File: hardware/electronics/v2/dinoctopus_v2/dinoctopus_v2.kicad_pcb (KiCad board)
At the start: 2 copper layers, 67 parts, among them J1 Conn_01x04_Socket, J1-I1 SJ-3524-SMT, J1-I2 SJ-3524-SMT, J1-I3 SJ-3524-SMT, J1-I4 SJ-3524-SMT, J1-I5 SJ-3524-SMT, J11-O1 SJ-3524-SMT, J11-O2 SJ-3524-SMT, J11-O3 SJ-3524-SMT, J11-O4 SJ-3524-SMT, J11-O5 SJ-3524-SMT, J2 Conn_01x03_Pin, U1 Pico mounting, U2 H11L1, U3 H11L1, U4 H11L1, U5 H11L1, U6 H11L1

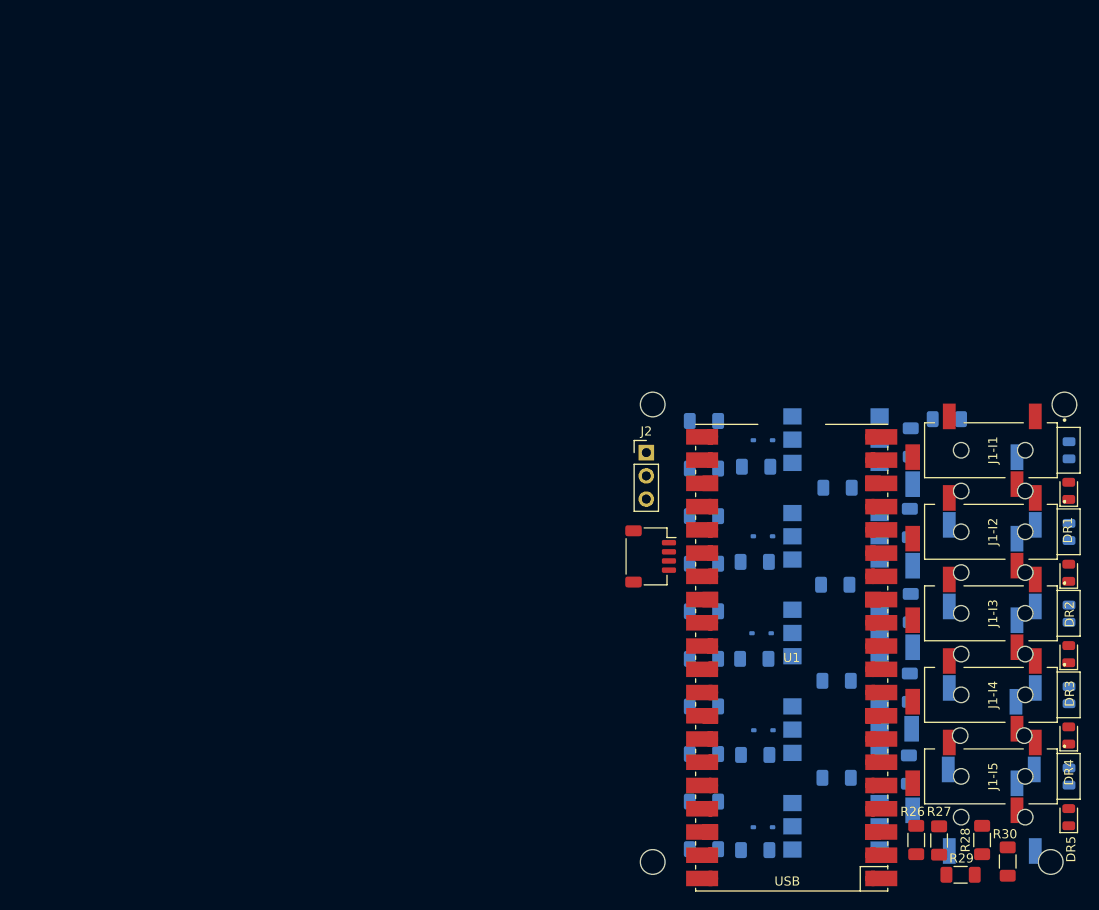
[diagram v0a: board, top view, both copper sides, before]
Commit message: Rework schemas with JLCPCB references
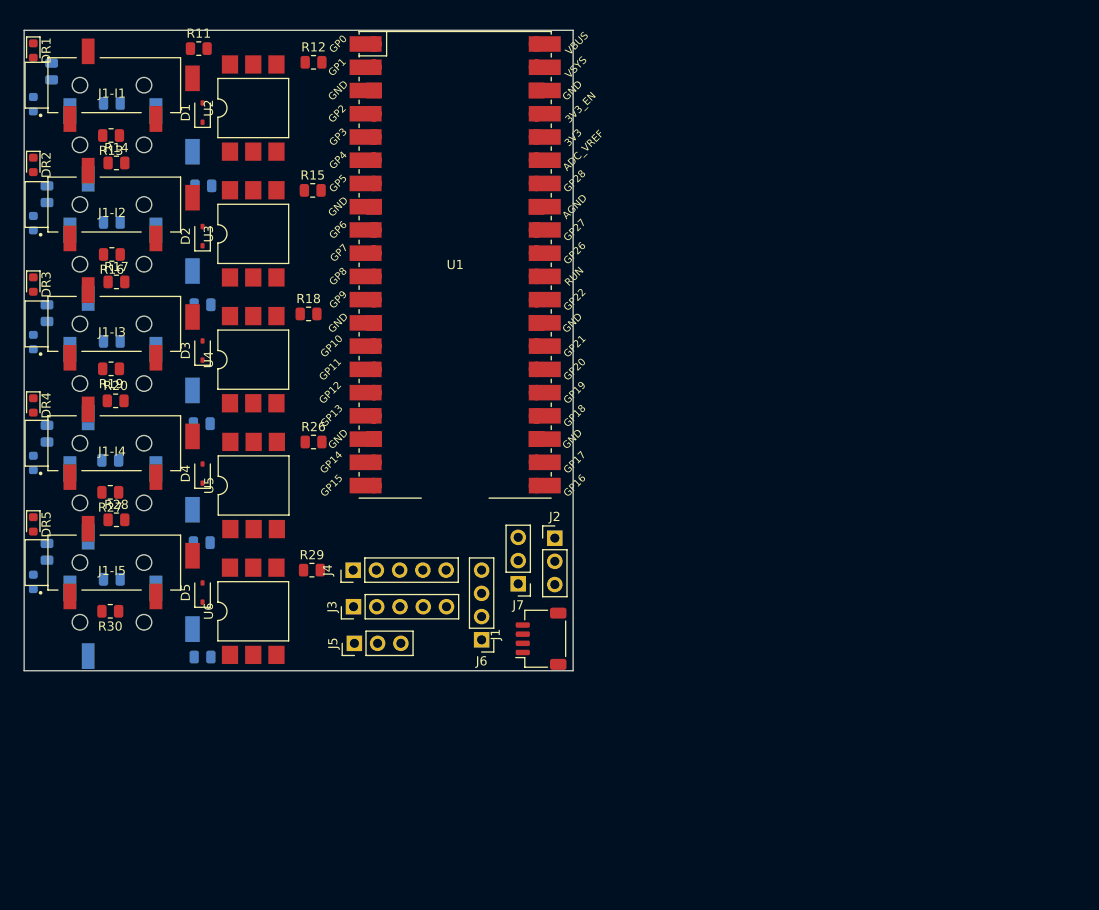
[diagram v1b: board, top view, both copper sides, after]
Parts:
- removed REF** (x4): MountingHole_2.7mm_M2.5, MountingHole:MountingHole_2.7mm_M2.5
- added J3: Conn_01x05_Pin, Connector_PinHeader_2.54mm:PinHeader_1x05_P2.54mm_Vertical, F.Cu at (63.0, 93.5)
- added J4: Conn_01x05_Pin, Connector_PinHeader_2.54mm:PinHeader_1x05_P2.54mm_Vertical, F.Cu at (63.0, 89.5)
- added J5: Conn_01x03_Pin, Connector_PinHeader_2.54mm:PinHeader_1x03_P2.54mm_Vertical, F.Cu at (63.1, 97.5)
- added J6: Conn_01x04_Pin, Connector_PinHeader_2.54mm:PinHeader_1x04_P2.54mm_Vertical, F.Cu at (77.0, 97.1)
- added J7: Conn_01x03_Pin, Connector_PinHeader_2.54mm:PinHeader_1x03_P2.54mm_Vertical, F.Cu at (81.0, 91.0)
- D1, D2, D3, D4, D5, U2, U3, U4, U5, U6: moved to F.Cu
- DR1, DR2, DR3, DR4, DR5, DT1, DT2, DT3, DT4, DT5: footprint LED_SMD:LED_0805_2012Metric -> LED_SMD:LED_0603_1608Metric
- J1: footprint MIDI_projects:JST_SH_SM04B-SRSS-TB_1x04-1MP_P1.00mm_Horizontal -> Library:JST_SH_SM04B-SRSS-TB_1x04-1MP_P1.00mm_Horizontal
- J1-I1, J1-I2, J1-I3, J1-I4, J1-I5, J11-O1, J11-O2, J11-O3, J11-O4, J11-O5: footprint MIDI_projects:CUI_SJ-3524-SMT -> Library:CUI_SJ-3524-SMT
- R1, R7: value 33 -> 2.2K; footprint Resistor_SMD:R_1206_3216Metric_Pad1.30x1.75mm_HandSolder -> Resistor_SMD:R_0805_2012Metric
- R10, R4: value 10 -> 2.2K; footprint Resistor_SMD:R_1206_3216Metric_Pad1.30x1.75mm_HandSolder -> Resistor_SMD:R_0805_2012Metric
- R11, R12, R17, R18: footprint Resistor_SMD:R_1206_3216Metric_Pad1.30x1.75mm_HandSolder -> Resistor_SMD:R_0805_2012Metric; moved to F.Cu
- R13, R19: value 220 -> 2.2K; footprint Resistor_SMD:R_1206_3216Metric_Pad1.30x1.75mm_HandSolder -> Resistor_SMD:R_0805_2012Metric; moved to F.Cu
- R14, R20: value 470 -> 220; footprint Resistor_SMD:R_1206_3216Metric_Pad1.30x1.75mm_HandSolder -> Resistor_SMD:R_0805_2012Metric; moved to F.Cu
- R15: value 220 -> 470; footprint Resistor_SMD:R_1206_3216Metric_Pad1.30x1.75mm_HandSolder -> Resistor_SMD:R_0805_2012Metric; moved to F.Cu
- R16: value 470 -> 2.2K; footprint Resistor_SMD:R_1206_3216Metric_Pad1.30x1.75mm_HandSolder -> Resistor_SMD:R_0805_2012Metric; moved to F.Cu
- R2, R8: value 10 -> 33; footprint Resistor_SMD:R_1206_3216Metric_Pad1.30x1.75mm_HandSolder -> Resistor_SMD:R_0805_2012Metric
- R21, R24: value 2.2K -> 33; footprint Resistor_SMD:R_1206_3216Metric_Pad1.30x1.75mm_HandSolder -> Resistor_SMD:R_0805_2012Metric
- R22, R25: value 2.2K -> 10; footprint Resistor_SMD:R_1206_3216Metric_Pad1.30x1.75mm_HandSolder -> Resistor_SMD:R_0805_2012Metric
- R23, R27, R30, R5, R6: footprint Resistor_SMD:R_1206_3216Metric_Pad1.30x1.75mm_HandSolder -> Resistor_SMD:R_0805_2012Metric
- R26, R29: value 2.2K -> 470; footprint Resistor_SMD:R_1206_3216Metric_Pad1.30x1.75mm_HandSolder -> Resistor_SMD:R_0805_2012Metric
- R28: value 2.2K -> 220; footprint Resistor_SMD:R_1206_3216Metric_Pad1.30x1.75mm_HandSolder -> Resistor_SMD:R_0805_2012Metric
- R3, R9: value 33 -> 10; footprint Resistor_SMD:R_1206_3216Metric_Pad1.30x1.75mm_HandSolder -> Resistor_SMD:R_0805_2012Metric
- U1: footprint MIDI_projects:RPi_Pico_SMD_Only -> Library:RPi_Pico_SMD_Only
- moved DT5 135.0 mm to (28.0, 38.6)
- moved J11-O5 126.8 mm to (33.1, 43.0), turned to 0 degrees
- moved DT4 124.4 mm to (28.0, 51.6)
- moved DR1 123.0 mm to (28.0, 32.7), turned to -90 degrees
- moved DR2 121.6 mm to (28.0, 45.2), turned to -90 degrees
- moved DR3 120.2 mm to (28.0, 58.3), turned to -90 degrees
- moved DR4 118.8 mm to (28.0, 71.5), turned to -90 degrees
- moved DR5 117.6 mm to (28.0, 84.5), turned to -90 degrees
- moved DT3 117.0 mm to (28.0, 64.6)
- moved J11-O4 115.3 mm to (33.1, 56.1), turned to 0 degrees
- moved DT1 114.1 mm to (28.0, 90.8)
- moved DT2 113.5 mm to (28.0, 77.8)
- moved J1-I1 110.7 mm to (33.1, 36.5), turned to 0 degrees
- moved J1-I2 109.3 mm to (33.1, 49.5), turned to 0 degrees
- moved J1-I3 108.0 mm to (33.1, 62.6), turned to 0 degrees
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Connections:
- J2 pad 1: Net-(J2-Pin_1) -> GND
- J2 pad 2: Net-(J2-Pin_2) -> +3V3
- R1 pad 2: Net-(J11-O1-Pad3) -> Net-(DT1-A)
- R10 pad 1: /Midi Output 5/TX -> +3V3
- R10 pad 2: Net-(J11-O5-Pad2) -> Net-(DT4-A)
- R13 pad 1: Net-(J1-I2-Pad3) -> +3V3
- R13 pad 2: Net-(D2-K) -> Net-(DR1-A)
- R14 pad 1: /MIDI input 2/RX -> Net-(J1-I2-Pad3)
- R14 pad 2: +3V3 -> Net-(D2-K)
- R15 pad 1: Net-(J1-I3-Pad3) -> /MIDI input 2/RX
- R15 pad 2: Net-(D3-K) -> +3V3
- R16 pad 1: /MIDI input 3/RX -> +3V3
- R16 pad 2: +3V3 -> Net-(DR2-A)
- R17 pad 1: Net-(J1-I4-Pad3) -> Net-(J1-I3-Pad3)
- R17 pad 2: Net-(D4-K) -> Net-(D3-K)
- R18 pad 1: /MIDI input 4/RX -> /MIDI input 3/RX
- R19 pad 1: Net-(J1-I5-Pad3) -> +3V3
- R19 pad 2: Net-(D5-K) -> Net-(DR3-A)
- R2 pad 1: /Midi Output 1/TX -> +3V3
- R2 pad 2: Net-(J11-O1-Pad2) -> Net-(J11-O1-Pad3)
- R20 pad 1: /MIDI input 5/RX -> Net-(J1-I4-Pad3)
- R20 pad 2: +3V3 -> Net-(D4-K)
- R21 pad 2: Net-(DT1-A) -> Net-(J11-O4-Pad3)
- R22 pad 1: +3V3 -> /Midi Output 4/TX
- R22 pad 2: Net-(DT2-A) -> Net-(J11-O4-Pad2)
- R23 pad 2: Net-(DT3-A) -> Net-(DT5-A)
- R24 pad 2: Net-(DT4-A) -> Net-(J11-O5-Pad3)
- R25 pad 1: +3V3 -> /Midi Output 5/TX
- R25 pad 2: Net-(DT5-A) -> Net-(J11-O5-Pad2)
- R26 pad 1: +3V3 -> /MIDI input 4/RX
- R26 pad 2: Net-(DR1-A) -> +3V3
- R27 pad 2: Net-(DR2-A) -> Net-(DR4-A)
- R28 pad 1: +3V3 -> Net-(J1-I5-Pad3)
- R28 pad 2: Net-(DR3-A) -> Net-(D5-K)
- R29 pad 1: +3V3 -> /MIDI input 5/RX
- R29 pad 2: Net-(DR4-A) -> +3V3
- R3 pad 1: +3V3 -> /Midi Output 1/TX
- R3 pad 2: Net-(J11-O2-Pad3) -> Net-(J11-O1-Pad2)
- R4 pad 1: /Midi Output 2/TX -> +3V3
- R4 pad 2: Net-(J11-O2-Pad2) -> Net-(DT2-A)
- R5 pad 2: Net-(J11-O3-Pad3) -> Net-(J11-O2-Pad3)
- R6 pad 1: /Midi Output 3/TX -> /Midi Output 2/TX
- R6 pad 2: Net-(J11-O3-Pad2) -> Net-(J11-O2-Pad2)
- R7 pad 2: Net-(J11-O4-Pad3) -> Net-(DT3-A)
- R8 pad 1: /Midi Output 4/TX -> +3V3
- R8 pad 2: Net-(J11-O4-Pad2) -> Net-(J11-O3-Pad3)
- R9 pad 1: +3V3 -> /Midi Output 3/TX
- R9 pad 2: Net-(J11-O5-Pad3) -> Net-(J11-O3-Pad2)
- U1 pad 10: unconnected-(U1-GPIO7-Pad10) -> Net-(J4-Pin_3)
- U1 pad 11: unconnected-(U1-GPIO8-Pad11) -> Net-(J4-Pin_4)
- U1 pad 12: unconnected-(U1-GPIO9-Pad12) -> Net-(J4-Pin_5)
- U1 pad 18: unconnected-(U1-GND-Pad18) -> Net-(J5-Pin_1)
- U1 pad 19: unconnected-(U1-GPIO14-Pad19) -> Net-(J5-Pin_2)
- U1 pad 20: unconnected-(U1-GPIO15-Pad20) -> Net-(J5-Pin_3)
- U1 pad 21: unconnected-(U1-GPIO16-Pad21) -> Net-(J6-Pin_1)
- U1 pad 22: unconnected-(U1-GPIO17-Pad22) -> Net-(J6-Pin_2)
- U1 pad 23: unconnected-(U1-GND-Pad23) -> Net-(J6-Pin_3)
- U1 pad 24: unconnected-(U1-GPIO18-Pad24) -> Net-(J6-Pin_4)
- U1 pad 3: unconnected-(U1-GND-Pad3) -> Net-(J3-Pin_1)
- U1 pad 33: unconnected-(U1-AGND-Pad33) -> Net-(J7-Pin_1)
- U1 pad 34: unconnected-(U1-GPIO28_ADC2-Pad34) -> Net-(J7-Pin_2)
- U1 pad 35: unconnected-(U1-ADC_VREF-Pad35) -> Net-(J7-Pin_3)
- U1 pad 4: unconnected-(U1-GPIO2-Pad4) -> Net-(J3-Pin_2)
- U1 pad 40: unconnected-(U1-VBUS-Pad40) -> Net-(J2-Pin_3)
- U1 pad 5: unconnected-(U1-GPIO3-Pad5) -> Net-(J3-Pin_3)
- U1 pad 6: unconnected-(U1-GPIO4-Pad6) -> Net-(J3-Pin_4)
- U1 pad 7: unconnected-(U1-GPIO5-Pad7) -> Net-(J3-Pin_5)
- U1 pad 8: unconnected-(U1-GND-Pad8) -> Net-(J4-Pin_1)
- U1 pad 9: unconnected-(U1-GPIO6-Pad9) -> Net-(J4-Pin_2)
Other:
- board outline added: 60 x 70 mm
- board text removed: "USB"

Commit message: giant mess
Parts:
- removed J2, J5, J7: Conn_01x03_Pin, Connector_PinHeader_2.54mm:PinHeader_1x03_P2.54mm_Vertical
- removed J6: Conn_01x04_Pin, Connector_PinHeader_2.54mm:PinHeader_1x04_P2.54mm_Vertical
- removed U1: Pico mounting, Library:RPi_Pico_SMD_Only
- DR1, DR2, DR3, DR4, DR5: footprint LED_SMD:LED_0603_1608Metric -> Library:rx_with_light_pipe
- DT1, DT2, DT3, DT4, DT5: footprint LED_SMD:LED_0603_1608Metric -> Library:tx_with_light_pipe; moved to F.Cu
- J3, J4: value Conn_01x05_Pin -> Conn_01x20_Pin; footprint Connector_PinHeader_2.54mm:PinHeader_1x05_P2.54mm_Vertical -> Connector_PinSocket_2.54mm:PinSocket_1x20_P2.54mm_Vertical
- R1, R10, R2, R21, R22, R23, R24, R25, R3, R4, R5, R6, R7, R8, R9: moved to F.Cu
- moved J3 62.8 mm to (51.2, 31.9), turned to 0 degrees
- moved J4 57.9 mm to (69.0, 31.9), turned to 0 degrees
- moved R4 27.1 mm to (55.9, 68.5)
- moved J1 15.7 mm to (68.0, 94.5), turned to 0 degrees
- moved R13 11.8 mm to (30.7, 31.8)
- moved R2 11.5 mm to (36.4, 93.5), turned to 0 degrees
- moved R27 11.4 mm to (30.9, 71.0)
- moved R3 11.1 mm to (28.0, 97.6), turned to -90 degrees
- moved U6 10.7 mm to (60.2, 87.1), turned to 0 degrees
- moved R21 10.7 mm to (37.1, 55.5), turned to 0 degrees
- moved R22 10.6 mm to (47.0, 53.6), turned to 90 degrees
- moved R24 10.6 mm to (37.1, 42.9), turned to 0 degrees
- moved R5 10.4 mm to (36.9, 82.1), turned to 0 degrees
- moved R8 10.4 mm to (37.0, 69.1)
- moved R16 10.1 mm to (37.1, 44.9), turned to 0 degrees
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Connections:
- J3 pad 1: Net-(J3-Pin_1) -> /Midi Output 5/TX
- J3 pad 2: Net-(J3-Pin_2) -> /MIDI input 5/RX
- J4 pad 3: Net-(J4-Pin_3) -> GND
- J4 pad 5: Net-(J4-Pin_5) -> +3V3
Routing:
- net /MIDI input 5/RX: track 0.00 -> 117.2 mm, vias 0 -> 2
- net /Midi Output 1/TX: track 0.00 -> 72.8 mm
- net /MIDI input 1/RX: track 0.00 -> 69.8 mm, vias 0 -> 1
- net /Midi Output 4/TX: track 0.00 -> 64.1 mm
- net /MIDI input 2/RX: track 0.00 -> 60.7 mm, vias 0 -> 2
- net /Midi Output 2/TX: track 0.00 -> 55.9 mm
- net /MIDI input 3/RX: track 0.00 -> 54.5 mm, vias 0 -> 1
- net /Midi Output 3/TX: track 0.00 -> 52.6 mm, vias 0 -> 1
- net /MIDI input 4/RX: track 0.00 -> 46.2 mm, vias 0 -> 2
- net Net-(J1-Pin_3): track 0.00 -> 42.4 mm
- net Net-(J1-Pin_4): track 0.00 -> 42.1 mm
- net /Midi Output 5/TX: track 0.00 -> 34.9 mm, vias 0 -> 1
- net Net-(DT2-A): track 0.00 -> 32.0 mm
- net Net-(D3-A): track 0.00 -> 29.6 mm, vias 0 -> 2
- net Net-(D1-A): track 0.00 -> 26.2 mm, vias 0 -> 2
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- added copper zone on In1.Cu, net +3V3
- added copper zone on In2.Cu, net GND
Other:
- board size 60 x 70 mm -> 45.5 x 71.5 mm
- copper layers 2 -> 4
- board text added: "JLCJLCJLCJLC"
- board text added: "dinoctopus - rev 2 bjonnh-midi@bjonnh.net"
